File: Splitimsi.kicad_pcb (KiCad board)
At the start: 2 copper layers, 118.2 x 99.3 mm, 30 parts, among them SW1 MX_RGB, SW10 MX_RGB, SW11 MX_RGB, SW12 MX_RGB, SW13 MX_RGB, SW14 MX_RGB, SW15 MX_RGB, SW16 MX_RGB, SW17 MX_RGB, SW18 MX_RGB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

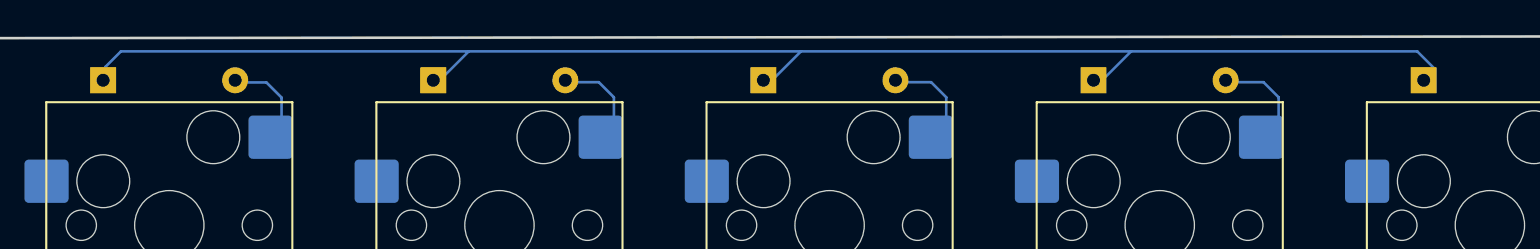
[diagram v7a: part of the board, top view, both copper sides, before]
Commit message: Rows and Columns labels connected to the MCU
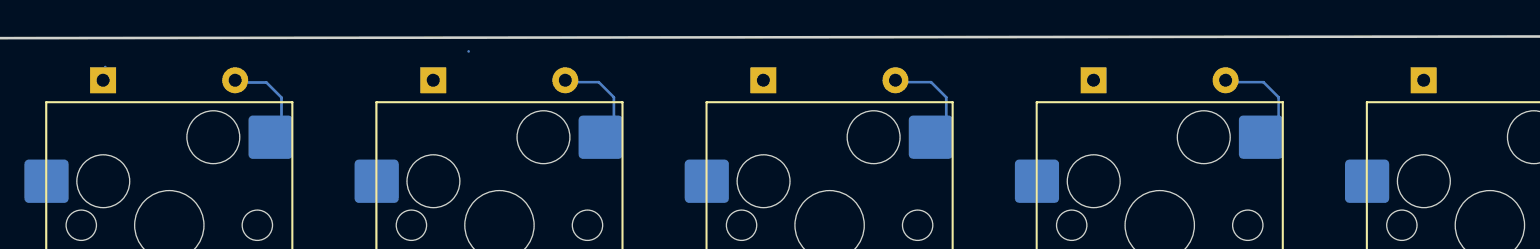
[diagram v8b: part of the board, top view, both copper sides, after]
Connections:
- U1 pad 10: unconnected-(U1-Pad10) -> /Col5
- U1 pad 11: unconnected-(U1-Pad11) -> /Row0
- U1 pad 12: unconnected-(U1-Pad12) -> /Row1
- U1 pad 13: unconnected-(U1-Pad13) -> /Row2
- U1 pad 14: unconnected-(U1-Pad14) -> /Row3
- U1 pad 15: unconnected-(U1-Pad15) -> /Row4
- U1 pad 5: unconnected-(U1-Pad5) -> /Col0
- U1 pad 6: unconnected-(U1-Pad6) -> /Col1
- U1 pad 7: unconnected-(U1-Pad7) -> /Col2
- U1 pad 8: unconnected-(U1-Pad8) -> /Col3
- U1 pad 9: unconnected-(U1-Pad9) -> /Col4
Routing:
- net /Row0: track 86.7 -> 1.83 mm
